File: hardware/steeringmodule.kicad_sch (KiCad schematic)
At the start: 14 parts, among them J101 Conn_01x02, J102 PotConnector, J103 Conn_01x02

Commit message: hardware: added 3D IMG archives and schematic PDF
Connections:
- net GNDPWR: now also J101.2 (Pin_2); no longer J101.1 (Pin_1)
- net HBRIDGE/VBAT: now also J101.1 (Pin_1); no longer J101.2 (Pin_2)
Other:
- moved on the sheet: H101, H102, H103, H104, H105, H106, H107, H108, J101

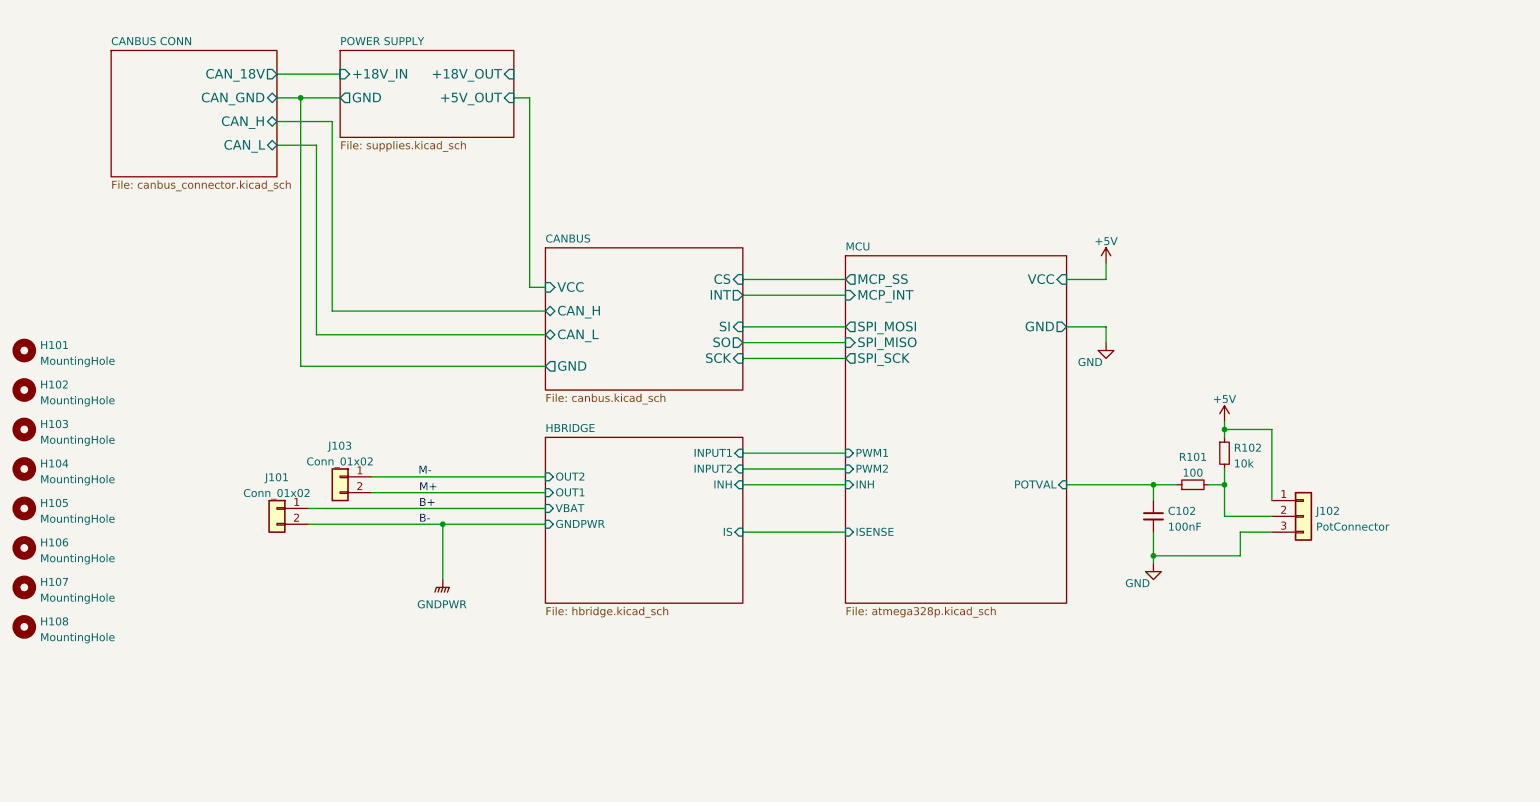
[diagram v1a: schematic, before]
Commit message: Added analog stage for Vbat measurement, and it's simulation
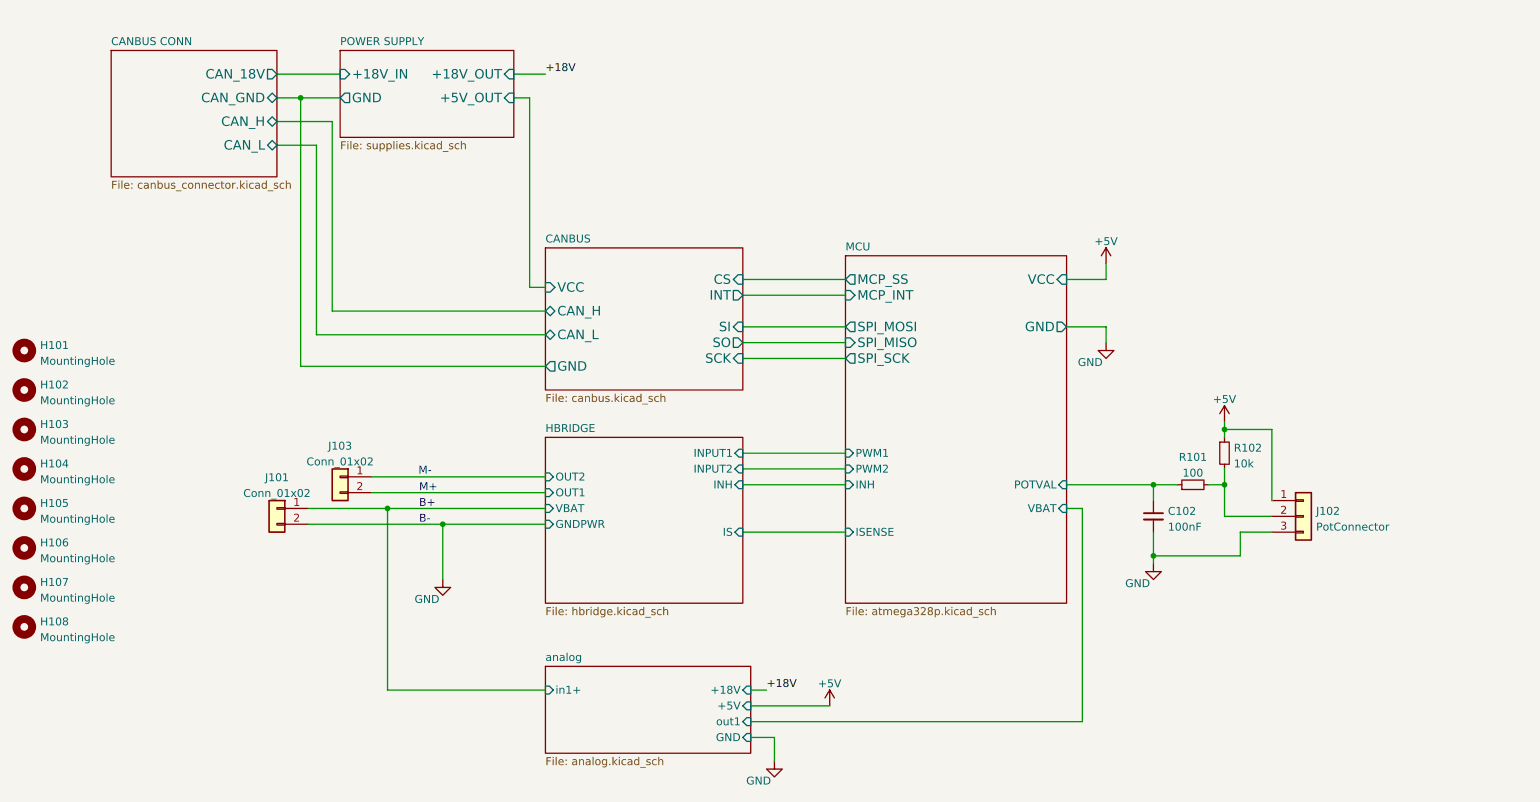
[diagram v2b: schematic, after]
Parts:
- J101, J103: footprint Connector_Phoenix_MSTB:PhoenixContact_MSTBA_2,5_2-G_1x02_P5.00mm_Horizontal -> Connector_Phoenix_MSTB:PhoenixContact_MSTBA_2,5_2-G-5,08_1x02_P5.08mm_Horizontal
- J102: footprint Connector_Phoenix_MSTB:PhoenixContact_MSTBA_2,5_3-G_1x03_P5.00mm_Horizontal -> Connector_Phoenix_MSTB:PhoenixContact_MSTBA_2,5_3-G-5,08_1x03_P5.08mm_Horizontal
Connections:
- net GNDPWR is gone; now on net GND: J101.2 (Pin_2)
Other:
- added sheet analog (analog.kicad_sch)
- sheet MCU ports: added VBAT; removed none

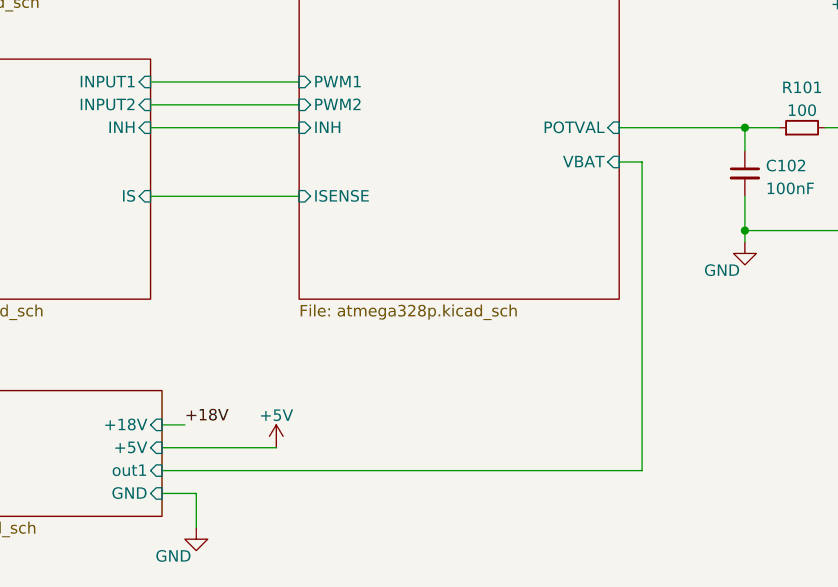
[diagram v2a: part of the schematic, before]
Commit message: Adjusted analog, now using INA826. Simulations updated.
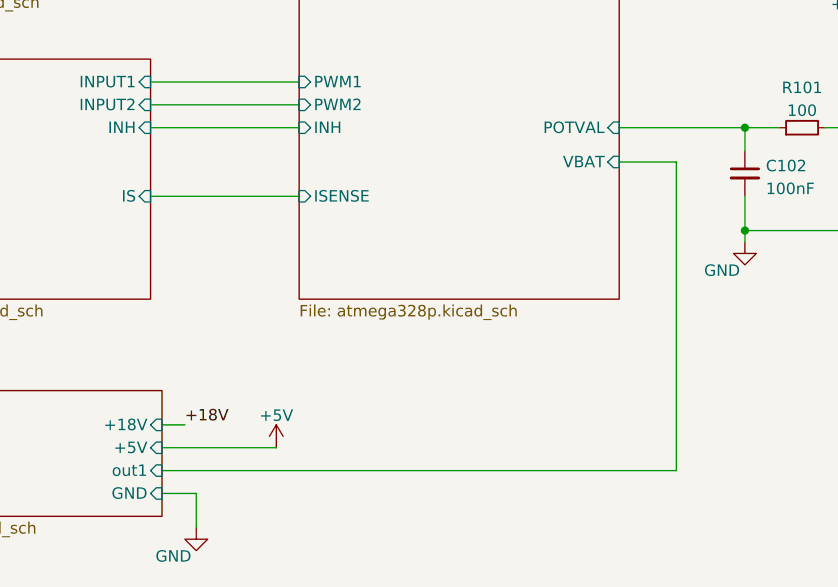
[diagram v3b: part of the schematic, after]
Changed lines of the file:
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@@
     (stroke (width 0) (type default) (color 0 0 0 0))
   )
-  (wire (pts (xy 199.39 106.68) (xy 199.39 140.97))
+  (wire (pts (xy 203.2 106.68) (xy 203.2 140.97))
     (stroke (width 0) (type default) (color 0 0 0 0))
   )
@@
     (stroke (width 0) (type default) (color 0 0 0 0))
   )
-  (wire (pts (xy 146.05 140.97) (xy 199.39 140.97))
+  (wire (pts (xy 146.05 140.97) (xy 203.2 140.97))
     (stroke (width 0) (type default) (color 0 0 0 0))
   )
@@
     (stroke (width 0) (type default) (color 0 0 0 0))
   )
-  (wire (pts (xy 196.85 106.68) (xy 199.39 106.68))
+  (wire (pts (xy 196.85 106.68) (xy 203.2 106.68))
     (stroke (width 0) (type default) (color 0 0 0 0))
   )
@@
       (reference "#PWR0602") (unit 1) (value "GND") (footprint "")
     )
-    (path "/cb531ef7-3b27-4a2f-a166-7c68e782adc2/8af2d5ad-70a9-494a-9383-a460dd63da52"
+    (path "/cb531ef7-3b27-4a2f-a166-7c68e782adc2/9d387373-bea2-4b66-8329-331f9647da70"
       (reference "#PWR0701") (unit 1) (value "GND") (footprint "")
     )
-    (path "/cb531ef7-3b27-4a2f-a166-7c68e782adc2/846025b9-03c1-4c5f-8732-c2176244c5c4"
+    (path "/cb531ef7-3b27-4a2f-a166-7c68e782adc2/6de9ee90-e48e-45a1-a090-6ba2b802c383"
       (reference "#PWR0702") (unit 1) (value "GND") (footprint "")
     )
-    (path "/cb531ef7-3b27-4a2f-a166-7c68e782adc2/e63ba045-3144-4bf0-9a1c-6e7c5df4af5b"
+    (path "/cb531ef7-3b27-4a2f-a166-7c68e782adc2/91ebc9b6-165d-4c10-8ddd-f50669161e92"
       (reference "#PWR0703") (unit 1) (value "GND") (footprint "")
     )
-    (path "/cb531ef7-3b27-4a2f-a166-7c68e782adc2/257ba76b-b4ba-415d-9845-f9d633f17fdb"
+    (path "/cb531ef7-3b27-4a2f-a166-7c68e782adc2/7c5689ec-d94d-480b-a335-f8bd31b53b3d"
       (reference "#PWR0704") (unit 1) (value "GND") (footprint "")
     )
@@
       (reference "#PWR0708") (unit 1) (value "GND") (footprint "")
     )
+    (path "/cb531ef7-3b27-4a2f-a166-7c68e782adc2/bb55eccf-8823-4a5b-9019-9d8f7ef9cb8f"
+      (reference "#PWR0709") (unit 1) (value "GND") (footprint "")
+    )
     (path "/51aee19b-ecda-41f3-b329-db9c4b1bc745"
       (reference "C102") (unit 1) (value "100nF") (footprint "Capacitor_SMD:C_0805_2012Metric_Pad1.18x1.45mm_HandSolder")
@@
       (reference "C603") (unit 1) (value "1uF") (footprint "Capacitor_SMD:C_1206_3216Metric_Pad1.33x1.80mm_HandSolder")
     )
-    (path "/cb531ef7-3b27-4a2f-a166-7c68e782adc2/754b0b53-25cd-473f-b6df-77d7505f205f"
-      (reference "C701") (unit 1) (value "100n") (footprint "Capacitor_SMD:C_0805_2012Metric_Pad1.18x1.45mm_HandSolder")
-    )
-    (path "/cb531ef7-3b27-4a2f-a166-7c68e782adc2/e1515b2a-5f9b-45c4-b663-445ec4103d55"
-      (reference "C702") (unit 1) (value "100n") (footprint "Capacitor_SMD:C_0805_2012Metric_Pad1.18x1.45mm_HandSolder")
-    )
-    (path "/cb531ef7-3b27-4a2f-a166-7c68e782adc2/1f79763d-f209-44ca-af1d-788097df1d36"
-      (reference "C703") (unit 1) (value "100n") (footprint "Capacitor_SMD:C_0805_2012Metric_Pad1.18x1.45mm_HandSolder")
+    (path "/cb531ef7-3b27-4a2f-a166-7c68e782adc2/5fb3777d-c6eb-4321-8783-2638327da882"
+      (reference "C701") (unit 1) (value "1n") (footprint "Capacitor_SMD:C_0805_2012Metric_Pad1.18x1.45mm_HandSolder")
+    )
+    (path "/cb531ef7-3b27-4a2f-a166-7c68e782adc2/54a4e543-8485-4c37-897a-e098611b8994"
+      (reference "C702") (unit 1) (value "1n") (footprint "Capacitor_SMD:C_0805_2012Metric_Pad1.18x1.45mm_HandSolder")
+    )
+    (path "/cb531ef7-3b27-4a2f-a166-7c68e782adc2/d1516051-2afd-4a2f-a1dc-6fdc650b7246"
+      (reference "C703") (unit 1) (value "1uF") (footprint "Capacitor_SMD:C_1206_3216Metric_Pad1.33x1.80mm_HandSolder")
     )
     (path "/cb531ef7-3b27-4a2f-a166-7c68e782adc2/526f9055-f514-46cc-8b8a-5e1f16375a31"
@@
       (reference "R405") (unit 1) (value "1k") (footprint "Resistor_SMD:R_0805_2012Metric_Pad1.20x1.40mm_HandSolder")
     )
-    (path "/cb531ef7-3b27-4a2f-a166-7c68e782adc2/15011e85-c327-46bd-b80d-265649c0a931"
-      (reference "R701") (unit 1) (value "10k") (footprint "Resistor_SMD:R_0805_2012Metric_Pad1.20x1.40mm_HandSolder")
-    )
-    (path "/cb531ef7-3b27-4a2f-a166-7c68e782adc2/67d293ff-6c0c-4bb7-bc9d-e47df64ee384"
-      (reference "R702") (unit 1) (value "10k") (footprint "Resistor_SMD:R_0805_2012Metric_Pad1.20x1.40mm_HandSolder")
-    )
-    (path "/cb531ef7-3b27-4a2f-a166-7c68e782adc2/09ee42d8-5e44-4653-a9e3-96b36db878fa"
-      (reference "R703") (unit 1) (value "10k") (footprint "Resistor_SMD:R_0805_2012Metric_Pad1.20x1.40mm_HandSolder")
-    )
-    (path "/cb531ef7-3b27-4a2f-a166-7c68e782adc2/3c1da6f1-5987-44f6-97b8-8f3d88b3dcef"
-      (reference "R704") (unit 1) (value "10k") (footprint "Resistor_SMD:R_0805_2012Metric_Pad1.20x1.40mm_HandSolder")
-    )
-    (path "/cb531ef7-3b27-4a2f-a166-7c68e782adc2/556e4a5f-40c3-4d72-9410-714bde1dc9bd"
-      (reference "R705") (unit 1) (value "11k") (footprint "Resistor_SMD:R_0805_2012Metric_Pad1.20x1.40mm_HandSolder")
-    )
-    (path "/cb531ef7-3b27-4a2f-a166-7c68e782adc2/51c0aba4-67d4-4c68-a0f5-c131bc9fee2f"
-      (reference "R706") (unit 1) (value "12k") (footprint "Resistor_SMD:R_0805_2012Metric_Pad1.20x1.40mm_HandSolder")
-    )
-    (path "/cb531ef7-3b27-4a2f-a166-7c68e782adc2/2148f2b6-facf-4495-acb4-dd632124e0f9"
-      (reference "R707") (unit 1) (value "12k") (footprint "Resistor_SMD:R_0805_2012Metric_Pad1.20x1.40mm_HandSolder")
-    )
-    (path "/cb531ef7-3b27-4a2f-a166-7c68e782adc2/b1fc89e4-a8a4-428c-b956-af765c4ae70b"
-      (reference "R708") (unit 1) (value "1k") (footprint "Resistor_SMD:R_0805_2012Metric_Pad1.20x1.40mm_HandSolder")
-    )
-    (path "/cb531ef7-3b27-4a2f-a166-7c68e782adc2/9b02f370-4aa1-4711-9fc1-1f37edfbd596"
-      (reference "R709") (unit 1) (value "1k") (footprint "Resistor_SMD:R_0805_2012Metric_Pad1.20x1.40mm_HandSolder")
-    )
-    (path "/cb531ef7-3b27-4a2f-a166-7c68e782adc2/d4ea8e9d-0a17-443b-8d08-e0718d0cbfd1"
-      (reference "R710") (unit 1) (value "1k") (footprint "Resistor_SMD:R_0805_2012Metric_Pad1.20x1.40mm_HandSolder")
+    (path "/cb531ef7-3b27-4a2f-a166-7c68e782adc2/c54bf9e7-79d2-4de4-a0eb-c5457dcb054e"
+      (reference "R701") (unit 1) (value "22k") (footprint "Resistor_SMD:R_0805_2012Metric_Pad1.20x1.40mm_HandSolder")
+    )
+    (path "/cb531ef7-3b27-4a2f-a166-7c68e782adc2/0a36eb84-3d8e-457d-a9c8-248f65c42b78"
+      (reference "R702") (unit 1) (value "22k") (footprint "Resistor_SMD:R_0805_2012Metric_Pad1.20x1.40mm_HandSolder")
+    )
+    (path "/cb531ef7-3b27-4a2f-a166-7c68e782adc2/eecc3b67-af5c-410e-a5d4-3ec9c9e43b2e"
+      (reference "R703") (unit 1) (value "8k2") (footprint "Resistor_SMD:R_0805_2012Metric_Pad1.20x1.40mm_HandSolder")
+    )
+    (path "/cb531ef7-3b27-4a2f-a166-7c68e782adc2/da7dfe37-67ab-4d8d-bbc7-091ffb6a6311"
+      (reference "R704") (unit 1) (value "8k2") (footprint "Resistor_SMD:R_0805_2012Metric_Pad1.20x1.40mm_HandSolder")
+    )
+    (path "/cb531ef7-3b27-4a2f-a166-7c68e782adc2/c951e989-ddbb-47a3-b7df-60d1dc4bfd52"
+      (reference "R705") (unit 1) (value "100") (footprint "Resistor_SMD:R_0805_2012Metric_Pad1.20x1.40mm_HandSolder")
     )
     (path "/91803bb3-8fed-4c45-ac45-15084f113b2a/6f7e3511-d093-4d47-b89e-cdbdada974a0"
@@
       (reference "TP702") (unit 1) (value "VBAT") (footprint "TestPoint:TestPoint_Pad_2.0x2.0mm")
     )
-    (path "/cb531ef7-3b27-4a2f-a166-7c68e782adc2/eda9daf8-4a7f-4ce2-b674-13d1c7c860fd"
-      (reference "TP703") (unit 1) (value "op_a_in-") (footprint "TestPoint:TestPoint_Pad_2.0x2.0mm")
-    )
-    (path "/cb531ef7-3b27-4a2f-a166-7c68e782adc2/61905c00-f230-448f-8a42-c2bb2b239b35"
-      (reference "TP704") (unit 1) (value "op_a_in+") (footprint "TestPoint:TestPoint_Pad_2.0x2.0mm")
-    )
-    (path "/cb531ef7-3b27-4a2f-a166-7c68e782adc2/90df661d-66cd-4956-9dbb-81da1f3bdad2"
-      (reference "TP705") (unit 1) (value "Vref") (footprint "TestPoint:TestPoint_Pad_2.0x2.0mm")
-    )
-    (path "/cb531ef7-3b27-4a2f-a166-7c68e782adc2/ea853174-c3b9-4253-8569-bd8ce3593d30"
-      (reference "TP706") (unit 1) (value "op_a_out") (footprint "TestPoint:TestPoint_Pad_2.0x2.0mm")
-    )
-    (path "/cb531ef7-3b27-4a2f-a166-7c68e782adc2/1ee86d84-a072-4535-bbc0-37f0e8277b88"
-      (reference "TP707") (unit 1) (value "op_b_in+") (footprint "TestPoint:TestPoint_Pad_2.0x2.0mm")
-    )
     (path "/cb531ef7-3b27-4a2f-a166-7c68e782adc2/a4498153-8a65-4663-b286-06ad3f9cc4a7"
-      (reference "TP708") (unit 1) (value "op_b_out") (footprint "TestPoint:TestPoint_Pad_2.0x2.0mm")
+      (reference "TP708") (unit 1) (value "out1") (footprint "TestPoint:TestPoint_Pad_2.0x2.0mm")
     )
     (path "/8cf6fa89-0a71-4daa-96aa-d68a3b21a66f/00000000-0000-0000-0000-000059fdaee3"
@@
       (reference "U602") (unit 1) (value "BTS7960B") (footprint "Package_TO_SOT_SMD:TO-263-7_TabPin8")
     )
-    (path "/cb531ef7-3b27-4a2f-a166-7c68e782adc2/bac9becd-632f-4018-befd-cf5eb74ecd6a"
-      (reference "U701") (unit 1) (value "LM324") (footprint "Package_SO:SOIC-14_3.9x8.7mm_P1.27mm")
-    )
-    (path "/cb531ef7-3b27-4a2f-a166-7c68e782adc2/61f8db63-6e8e-4258-ad83-bbd4865253ee"
-      (reference "U701") (unit 2) (value "LM324") (footprint "Package_SO:SOIC-14_3.9x8.7mm_P1.27mm")
-    )
-    (path "/cb531ef7-3b27-4a2f-a166-7c68e782adc2/9107f90e-86a8-40ce-9b18-211cf27a70d8"
-      (reference "U701") (unit 3) (value "LM324") (footprint "Package_SO:SOIC-14_3.9x8.7mm_P1.27mm")
-    )
-    (path "/cb531ef7-3b27-4a2f-a166-7c68e782adc2/564e0548-0b45-4144-b2e8-e008f64c83b0"
-      (reference "U701") (unit 5) (value "LM324") (footprint "Package_SO:SOIC-14_3.9x8.7mm_P1.27mm")
+    (path "/cb531ef7-3b27-4a2f-a166-7c68e782adc2/41cff564-36fc-4163-9a20-c7aaf039d3c9"
+      (reference "U701") (unit 1) (value "INA826_D_8") (footprint "Package_SO:SOIC-8_3.9x4.9mm_P1.27mm")
     )
     (path "/638e7cda-f2b7-4bba-84db-158f1b89b212/00000000-0000-0000-0000-000059fe3a5a"

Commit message: hardware: K78L15 to supply INA826 and other changes
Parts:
- added LOGO101: Logo_Open_Hardware_Small, Symbol:OSHW-Logo2_7.3x6mm_SilkScreen, symbol Graphic:Logo_Open_Hardware_Small
- added SYM101, SYM102: SYM_Flash_Small, KicadZeniteSolarLibrary18:symbol_logoZenite, symbol Graphic:SYM_Flash_Small
- added SYM103, SYM104: SYM_Flash_Small, KicadZeniteSolarLibrary18:synbol_logoifsc, symbol Graphic:SYM_Flash_Small
- added SYM105: SYM_Radioactive_Radiation_Small, KicadZeniteSolarLibrary18:symbol_naolavar, symbol Graphic:SYM_Radioactive_Radiation_Small
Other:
- sheet HBRIDGE ports: added IS1, IS2; removed IS
- sheet MCU ports: added ISENSE1, ISENSE2; removed ISENSE
- sheet POWER SUPPLY ports: added +15V; removed none
- sheet analog ports: added +15V; removed +18V, +5V
- note added: "(top and bottom)"
- note added: "Logo IFSC"
- note added: "Logo Zênite"
